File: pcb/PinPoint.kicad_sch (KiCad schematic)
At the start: 6 parts, among them U1 E73-2G4M08S-52833

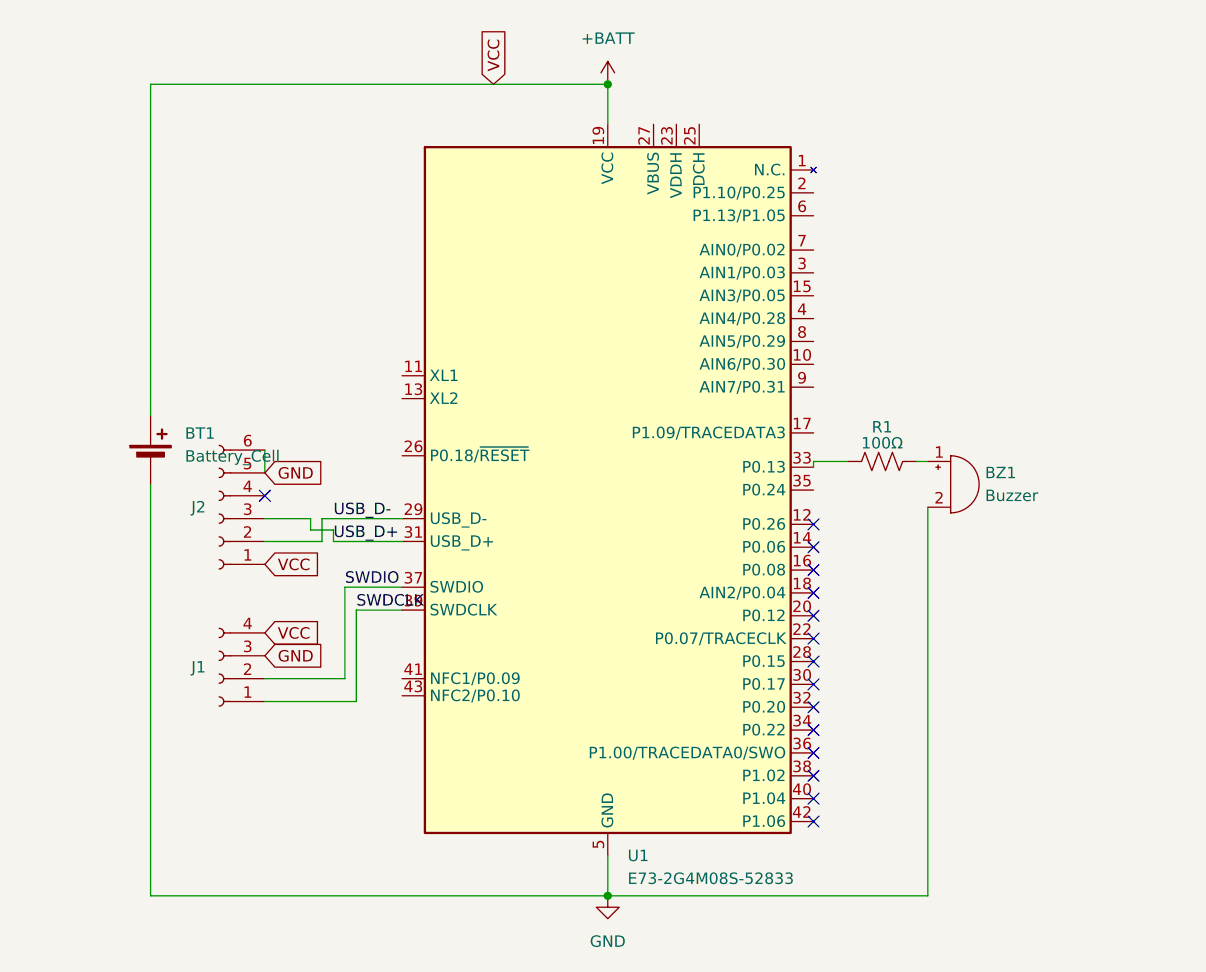
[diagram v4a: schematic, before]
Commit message: Complete board, add fab outputs
Signed-off-by: Devnol <pgkoutsoumanis@gmail.com>
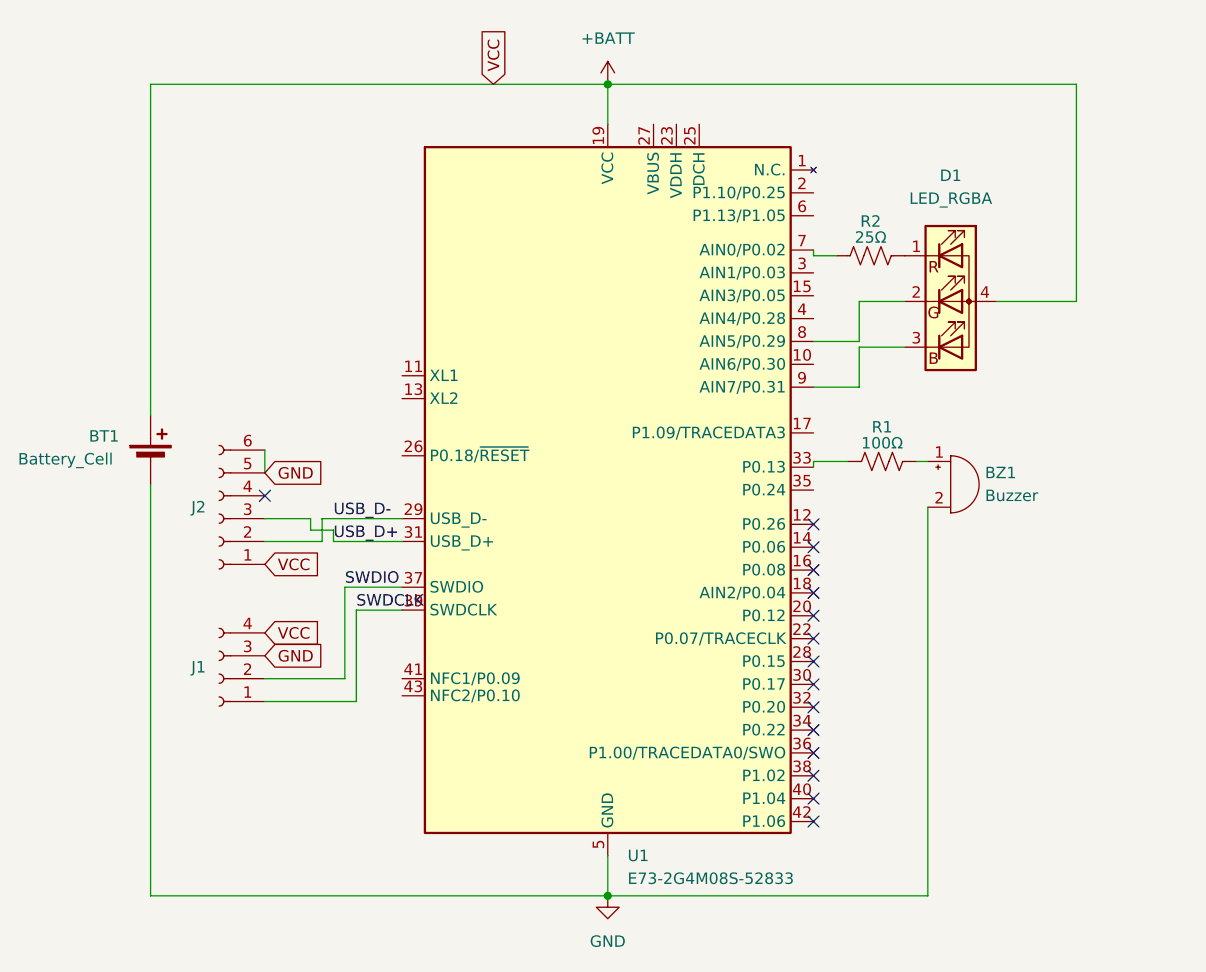
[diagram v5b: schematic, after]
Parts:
- added D1: LED_RGBA, LED_SMD:LED_LiteOn_LTST-C19HE1WT, symbol Device:LED_RGBA
- added R2: 25Ω, Resistor_SMD:R_0603_1608Metric, symbol Device:R_US
- J1: now left out of the parts list
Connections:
- net +BATT: now also D1.4 (A)
- net at U1.7 (AIN0/P0.02): now also R2.1
- net at U1.8 (AIN5/P0.29): now also D1.2 (GK)
- net at U1.9 (AIN7/P0.31): now also D1.3 (BK)
- new net: D1.1 (RK), R2.2
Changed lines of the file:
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@@
+	(wire
+		(pts
+			(xy 143.51 68.58) (xy 138.43 68.58)
+		)
+		(stroke
+			(width 0)
+			(type default)
+		)
+	)
+	(wire
+		(pts
+			(xy 162.56 68.58) (xy 153.67 68.58)
+		)
+		(stroke
+			(width 0)
+			(type default)
+		)
+	)
 	(wire
 		(pts
@@
 	(wire
 		(pts
+			(xy 138.43 73.025) (xy 133.35 73.025)
+		)
+		(stroke
+			(width 0)
+			(type default)
+		)
+	)
+	(wire
+		(pts
+			(xy 110.49 44.45) (xy 162.56 44.45)
+		)
+		(stroke
+			(width 0)
+			(type default)
+		)
+	)
+	(wire
+		(pts
 			(xy 81.28 110.49) (xy 81.28 100.33)
 		)
@@
 	(wire
 		(pts
+			(xy 138.43 73.66) (xy 138.43 78.105)
+		)
+		(stroke
+			(width 0)
+			(type default)
+		)
+	)
+	(wire
+		(pts
 			(xy 80.01 95.25) (xy 87.63 95.25)
 		)
@@
 	(wire
 		(pts
+			(xy 133.35 63.5) (xy 133.35 62.865)
+		)
+		(stroke
+			(width 0)
+			(type default)
+		)
+	)
+	(wire
+		(pts
 			(xy 144.78 86.36) (xy 146.05 86.36)
 		)
@@
 	(wire
 		(pts
+			(xy 162.56 44.45) (xy 162.56 68.58)
+		)
+		(stroke
+			(width 0)
+			(type default)
+		)
+	)
+	(wire
+		(pts
+			(xy 135.89 63.5) (xy 133.35 63.5)
+		)
+		(stroke
+			(width 0)
+			(type default)
+		)
+	)
+	(wire
+		(pts
 			(xy 59.69 134.62) (xy 110.49 134.62)
 		)
@@
 	(wire
 		(pts
+			(xy 138.43 78.105) (xy 133.35 78.105)
+		)
+		(stroke
+			(width 0)
+			(type default)
+		)
+	)
+	(wire
+		(pts
 			(xy 81.28 100.33) (xy 87.63 100.33)
 		)
@@
 	(wire
 		(pts
+			(xy 138.43 68.58) (xy 138.43 73.025)
+		)
+		(stroke
+			(width 0)
+			(type default)
+		)
+	)
+	(wire
+		(pts
 			(xy 80.01 93.98) (xy 80.01 95.25)
 		)
@@
 		(pts
 			(xy 78.74 92.71) (xy 78.74 95.25)
+		)
+		(stroke
+			(width 0)
+			(type default)
+		)
+	)
+	(wire
+		(pts
+			(xy 143.51 73.66) (xy 138.43 73.66)
 		)
 		(stroke
@@
 	)
 	(symbol
+		(lib_id "Device:LED_RGBA")
+		(at 148.59 68.58 0)
+		(unit 1)
+		(exclude_from_sim no)
+		(in_bom yes)
+		(on_board yes)
+		(dnp no)
+		(property "Reference" "D1"
+			(at 148.59 54.61 0)
+			(effects
+				(font
+					(size 1.27 1.27)
+				)
+			)
+		)
+		(property "Value" "LED_RGBA"
+			(at 148.59 57.15 0)
+			(effects
+				(font
+					(size 1.27 1.27)
+				)
+			)
+		)
+		(property "Footprint" "LED_SMD:LED_LiteOn_LTST-C19HE1WT"
+			(at 148.59 69.85 0)
+			(effects
+				(font
+					(size 1.27 1.27)
+				)
+				(hide yes)
+			)
+		)
+		(property "Datasheet" "~"
+			(at 148.59 69.85 0)
+			(effects
+				(font
+					(size 1.27 1.27)
+				)
+				(hide yes)
+			)
+		)
+		(property "Description" "RGB LED, red/green/blue/anode"
+			(at 148.59 68.58 0)
+			(effects
+				(font
+					(size 1.27 1.27)
+				)
+				(hide yes)
+			)
+		)
+		(pin "2"
+		)
+		(pin "1"
+		)
+		(pin "3"
+		)
+		(pin "4"
+		)
+		(instances
+			(project ""
+				(path "/cd1943be-3de8-48d0-ac34-bcd8bf7ade3c"
+					(reference "D1")
+					(unit 1)
+				)
+			)
+		)
+	)
+	(symbol
 		(lib_id "Connector:Conn_01x06_Socket")
 		(at 67.31 92.71 180)
@@
 		(on_board yes)
 		(dnp no)
-		(fields_autoplaced yes)
 		(property "Reference" "BT1"
-			(at 63.5 83.2484 0)
+			(at 52.832 83.566 0)
 			(effects
 				(font
@@
 		)
 		(property "Value" "Battery_Cell"
-			(at 63.5 85.7884 0)
+			(at 44.958 86.106 0)
 			(effects
 				(font
@@
 		(unit 1)
 		(exclude_from_sim no)
-		(in_bom yes)
+		(in_bom no)
 		(on_board yes)
 		(dnp no)
@@
 					(unit 1)
 				)
+			)
+		)
+	)
+	(symbol
+		(lib_id "Device:R_US")
+		(at 139.7 63.5 90)
+		(unit 1)
+		(exclude_from_sim no)
+		(in_bom yes)
+		(on_board yes)
+		(dnp no)
+		(property "Reference" "R2"
+			(at 139.7 59.69 90)
+			(effects
+				(font
+					(size 1.27 1.27)
+				)
+			)
+		)
+		(property "Value" "25Ω"
+			(at 139.7 61.468 90)
+			(effects
+				(font
+					(size 1.27 1.27)
+				)
+			)
+		)
+		(property "Footprint" "Resistor_SMD:R_0603_1608Metric"
+			(at 139.954 62.484 90)
+			(effects
+				(font
+					(size 1.27 1.27)
+				)
+				(hide yes)
+			)
+		)
+		(property "Datasheet" "~"
+			(at 139.7 63.5 0)
+			(effects
+				(font
+					(size 1.27 1.27)
+				)
+				(hide yes)
+			)
+		)
+		(property "Description" "Resistor, US symbol"
+			(at 139.7 63.5 0)
+			(effects
+				(font
+					(size 1.27 1.27)
+				)
+				(hide yes)
+			)
+		)
+		(pin "2"
+		)
+		(pin "1"
+		)
+		(instances
+			(project "PinPoint"
+				(path "/cd1943be-3de8-48d0-ac34-bcd8bf7ade3c"
+					(reference "R2")
+					(unit 1)
+				)

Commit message: Add push button
Signed-off-by: Devnol <pgkoutsoumanis@gmail.com>
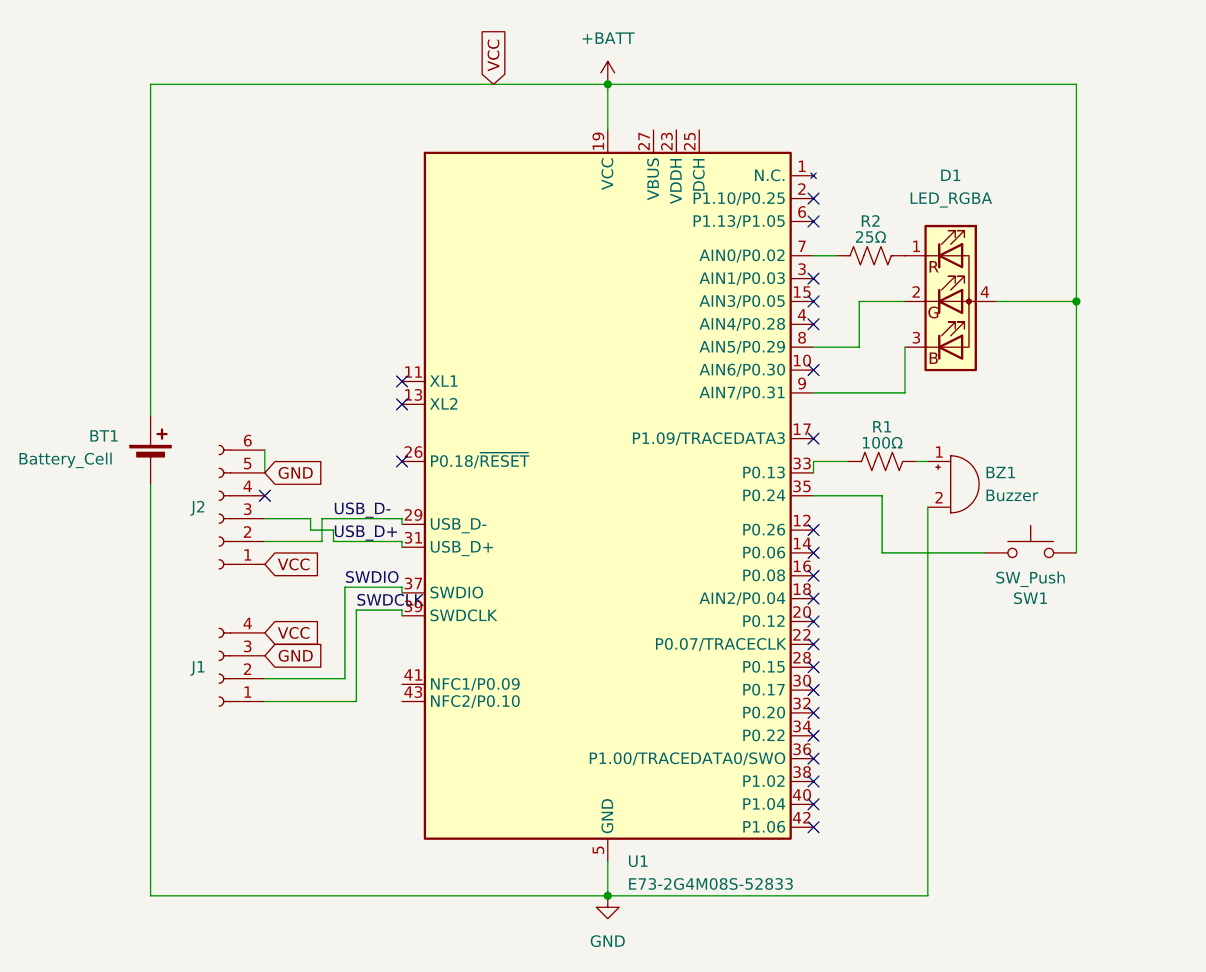
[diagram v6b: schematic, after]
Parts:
- added SW1: SW_Push, Button_Switch_SMD:SW_SPST_CK_KXT3, symbol Switch:SW_Push
- BT1: LCSC Part # (none) -> C964823
- BZ1: LCSC Part # (none) -> C910763
- D1: LCSC Part # (none) -> C458749
- J2: LCSC Part # (none) -> C132560
- U1: LCSC Part # (none) -> C356849
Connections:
- net +BATT: now also SW1.2
- net at U1.35 (P0.24): now also SW1.1
- no-connect marks 15 -> 25
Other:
- moved on the sheet: U1

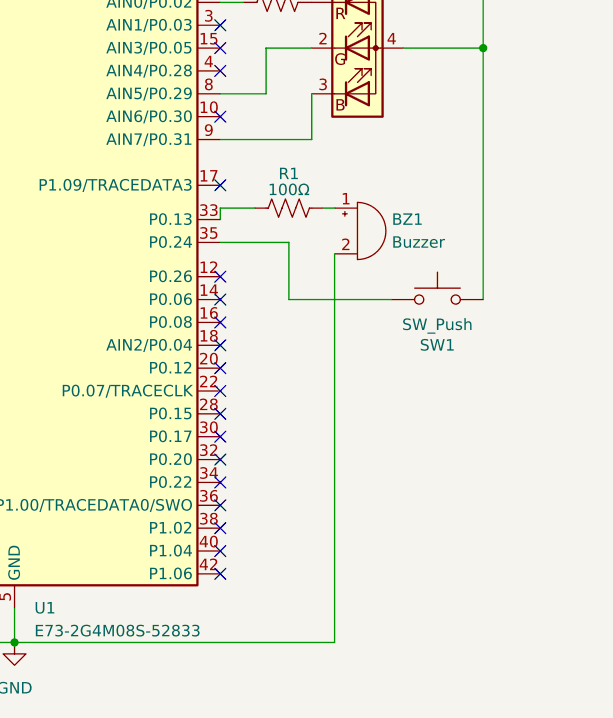
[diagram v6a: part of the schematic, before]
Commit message: Replace buzzer for active Add missing 3d models from lcsc
Signed-off-by: Devnol <pgkoutsoumanis@gmail.com>
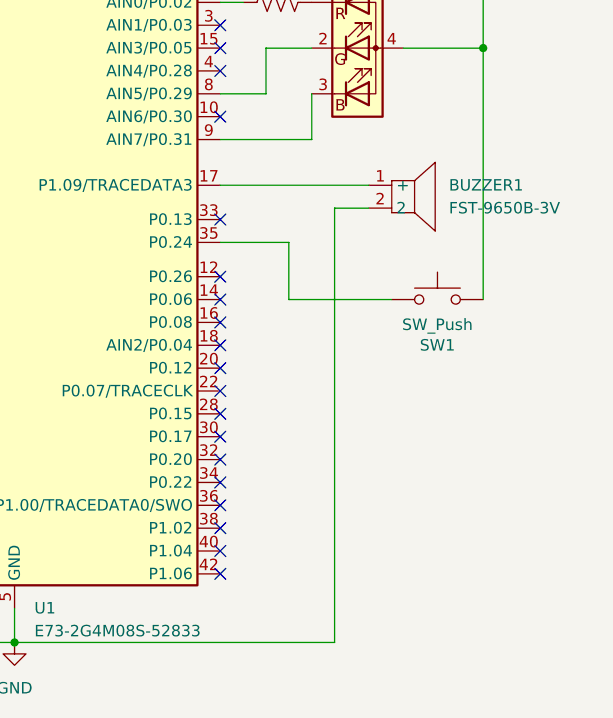
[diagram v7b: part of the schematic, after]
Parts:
- removed BZ1: Buzzer, Buzzer_Beeper:Buzzer_Murata_PKMCS0909E, symbol Device:Buzzer
- removed R1: 100Ω, Resistor_SMD:R_0603_1608Metric, symbol Device:R_US
- added BUZZER1: FST-9650B-3V, PinPoint_lib:BUZ-SMD_L9.6-W9.6-LS10.0-R, symbol PinPoint_lib:FST-9650B-3V
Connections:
- net GND: now also BUZZER1.2
- net at U1.17 (P1.09/TRACEDATA3): now also BUZZER1.1 (+)
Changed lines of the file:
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@@
 	)
 	(no_connect
-		(at 133.35 83.82)
+		(at 133.35 87.63)
 	)
 	(no_connect
@@
 	(wire
 		(pts
-			(xy 133.35 86.36) (xy 133.35 87.63)
-		)
-		(stroke
-			(width 0)
-			(type default)
-		)
-	)
-	(wire
-		(pts
 			(xy 80.01 95.25) (xy 87.63 95.25)
 		)
@@
 	(wire
 		(pts
-			(xy 144.78 86.36) (xy 146.05 86.36)
-		)
-		(stroke
-			(width 0)
-			(type default)
-		)
-	)
-	(wire
-		(pts
 			(xy 162.56 44.45) (xy 162.56 68.58)
 		)
@@
 	(wire
 		(pts
+			(xy 133.35 83.82) (xy 149.86 83.82)
+		)
+		(stroke
+			(width 0)
+			(type default)
+		)
+	)
+	(wire
+		(pts
+			(xy 146.05 86.36) (xy 149.86 86.36)
+		)
+		(stroke
+			(width 0)
+			(type default)
+		)
+	)
+	(wire
+		(pts
 			(xy 87.63 92.71) (xy 87.63 93.345)
 		)
@@
 	(wire
 		(pts
-			(xy 146.05 91.44) (xy 146.05 134.62)
-		)
-		(stroke
-			(width 0)
-			(type default)
-		)
-	)
-	(wire
-		(pts
-			(xy 133.35 86.36) (xy 137.16 86.36)
+			(xy 146.05 86.36) (xy 146.05 134.62)
 		)
 		(stroke
@@
 				(justify left)
 				(hide yes)
-			)
-		)
-	)
-	(symbol
-		(lib_id "Device:R_US")
-		(at 140.97 86.36 90)
-		(unit 1)
-		(exclude_from_sim no)
-		(in_bom yes)
-		(on_board yes)
-		(dnp no)
-		(property "Reference" "R1"
-			(at 140.97 82.55 90)
-			(effects
-				(font
-					(size 1.27 1.27)
-				)
-			)
-		)
-		(property "Value" "100Ω"
-			(at 140.97 84.328 90)
-			(effects
-				(font
-					(size 1.27 1.27)
-				)
-			)
-		)
-		(property "Footprint" "Resistor_SMD:R_0603_1608Metric"
-			(at 141.224 85.344 90)
-			(effects
-				(font
-					(size 1.27 1.27)
-				)
-				(hide yes)
-			)
-		)
-		(property "Datasheet" "~"
-			(at 140.97 86.36 0)
-			(effects
-				(font
-					(size 1.27 1.27)
-				)
-				(hide yes)
-			)
-		)
-		(property "Description" "Resistor, US symbol"
-			(at 140.97 86.36 0)
-			(effects
-				(font
-					(size 1.27 1.27)
-				)
-				(hide yes)
-			)
-		)
-		(property "LCSC Part #" ""
-			(at 140.97 86.36 0)
-			(effects
-				(font
-					(size 1.27 1.27)
-				)
-				(hide yes)
-			)
-		)
-		(pin "2"
-		)
-		(pin "1"
-		)
-		(instances
-			(project ""
-				(path "/cd1943be-3de8-48d0-ac34-bcd8bf7ade3c"
-					(reference "R1")
-					(unit 1)
-				)
 			)
 		)
@@
 				(path "/cd1943be-3de8-48d0-ac34-bcd8bf7ade3c"
 					(reference "J2")
-					(unit 1)
-				)
-			)
-		)
-	)
-	(symbol
-		(lib_id "Device:Buzzer")
-		(at 148.59 88.9 0)
-		(unit 1)
-		(exclude_from_sim no)
-		(in_bom yes)
-		(on_board yes)
-		(dnp no)
-		(fields_autoplaced yes)
-		(property "Reference" "BZ1"
-			(at 152.4 87.6299 0)
-			(effects
-				(font
-					(size 1.27 1.27)
-				)
-				(justify left)
-			)
-		)
-		(property "Value" "Buzzer"
-			(at 152.4 90.1699 0)
-			(effects
-				(font
-					(size 1.27 1.27)
-				)
-				(justify left)
-			)
-		)
-		(property "Footprint" "Buzzer_Beeper:Buzzer_Murata_PKMCS0909E"
-			(at 147.955 86.36 90)
-			(effects
-				(font
-					(size 1.27 1.27)
-				)
-				(hide yes)
-			)
-		)
-		(property "Datasheet" "~"
-			(at 147.955 86.36 90)
-			(effects
-				(font
-					(size 1.27 1.27)
-				)
-				(hide yes)
-			)
-		)
-		(property "Description" "Buzzer, polarized"
-			(at 148.59 88.9 0)
-			(effects
-				(font
-					(size 1.27 1.27)
-				)
-				(hide yes)
-			)
-		)
-		(property "LCSC Part #" "C910763"
-			(at 148.59 88.9 0)
-			(effects
-				(font
-					(size 1.27 1.27)
-				)
-				(hide yes)
-			)
-		)
-		(pin "2"
-		)
-		(pin "1"
-		)
-		(instances
-			(project ""
-				(path "/cd1943be-3de8-48d0-ac34-bcd8bf7ade3c"
-					(reference "BZ1")
 					(unit 1)
 				)
@@
 					(unit 1)
 				)
+			)
+		)
+	)
+	(symbol
+		(lib_id "PinPoint_lib:FST-9650B-3V")
+		(at 152.4 86.36 0)
+		(unit 1)
+		(exclude_from_sim no)
+		(in_bom yes)
+		(on_board yes)
+		(dnp no)
+		(fields_autoplaced yes)
+		(property "Reference" "BUZZER1"
+			(at 158.75 83.8199 0)
+			(effects
+				(font
+					(size 1.27 1.27)
+				)
+				(justify left)
+			)
+		)
+		(property "Value" "FST-9650B-3V"
+			(at 158.75 86.3599 0)
+			(effects
+				(font
+					(size 1.27 1.27)
+				)
+				(justify left)
+			)
+		)
+		(property "Footprint" "PinPoint_lib:BUZ-SMD_L9.6-W9.6-LS10.0-R"
+			(at 152.4 93.98 0)
+			(effects
+				(font
+					(size 1.27 1.27)
+				)
+				(hide yes)
+			)
+		)
+		(property "Datasheet" "https://lcsc.com/product-detail/Buzzers_FST-FST-9650B-3V_C391032.html"
+			(at 152.4 96.52 0)
+			(effects
+				(font
+					(size 1.27 1.27)
+				)
+				(hide yes)
+			)
+		)
+		(property "Description" ""
+			(at 152.4 86.36 0)
+			(effects
+				(font
+					(size 1.27 1.27)
+				)
+				(hide yes)
+			)
+		)
+		(property "LCSC Part" "C391032"
+			(at 152.4 99.06 0)
+			(effects
+				(font
+					(size 1.27 1.27)
+				)
+				(hide yes)
+			)
+		)
+		(property "LCSC Part #" "C391032"
+			(at 152.4 86.36 0)
+			(effects
+				(font
+					(size 1.27 1.27)
+				)
+				(hide yes)
+			)
+		)
+		(pin "2"
+		)
+		(pin "1"
+		)
+		(instances
+			(project ""
+				(path "/cd1943be-3de8-48d0-ac34-bcd8bf7ade3c"
+					(reference "BUZZER1")
+					(unit 1)
+				)
